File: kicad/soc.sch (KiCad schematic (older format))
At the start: 60 parts, among them J1 Line Out, J2 PS/2 Keyboard, J3 DB9, J4 Line In, J5 Headphone, P1 LED MATRIX, P2 ALTERA_DE1_GPIO, P3 IO, U1 SSM2603, U2 DS3234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

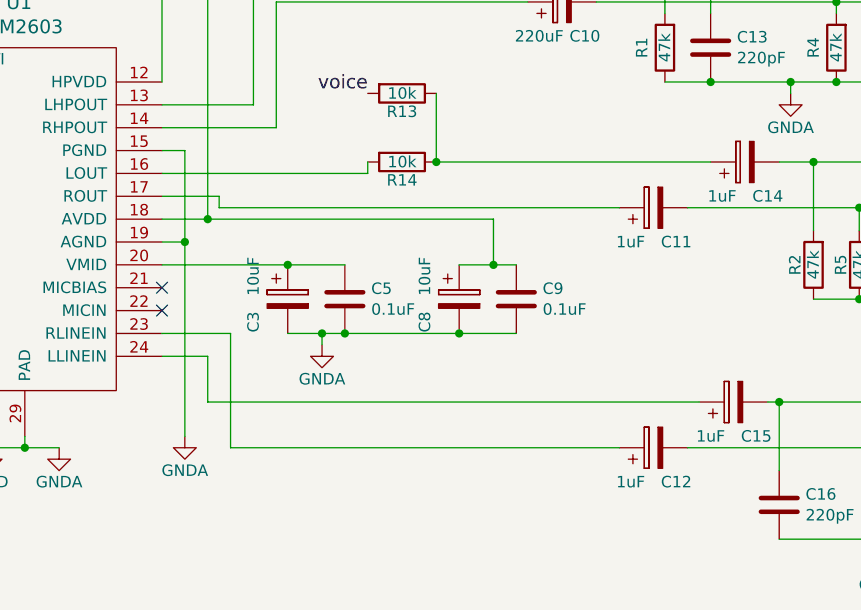
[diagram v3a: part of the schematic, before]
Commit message: additions to the support board
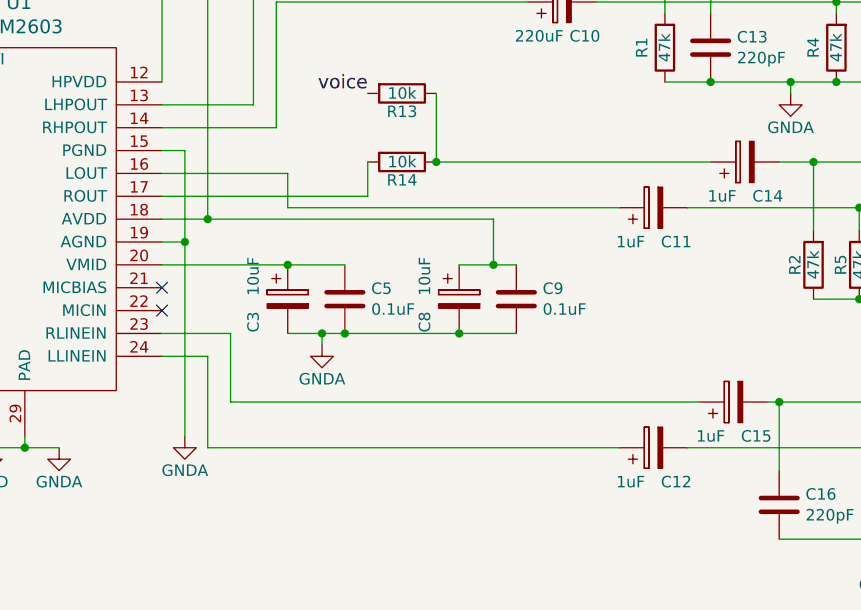
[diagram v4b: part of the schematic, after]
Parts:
- J3: footprint (none) -> mstock-pretty:DB9F
- J5: footprint (none) -> mstock-pretty:SJ-4351X-SMT
- U4: footprint (none) -> mstock-pretty:SOIC-16
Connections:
- net at U1.16 (LOUT): now also C11.1; no longer R14.2
- net at U1.17 (ROUT): now also R14.2; no longer C11.1
- net at U1.23 (RLINEIN): now also C15.1; no longer C12.1
- net at U1.24 (LLINEIN): now also C12.1; no longer C15.1
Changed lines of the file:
@@
 Connection ~ 8600 4300
 Wire Wire Line
-	5550 4150 6450 4150
-Wire Wire Line
-	5800 4300 7550 4300
-Wire Wire Line
-	5800 4300 5800 4250
-Wire Wire Line
-	5800 4250 5550 4250
+	6450 4250 5550 4250
 Wire Wire Line
 	7750 3750 9150 3750
@@
 Connection ~ 8700 5350
 Wire Wire Line
-	5750 5150 7900 5150
-Wire Wire Line
-	5850 5350 7550 5350
+	5750 5350 7550 5350
 Wire Wire Line
 	1750 2600 1250 2600
@@
 $EndComp
 Wire Wire Line
-	6450 4150 6450 4100
+	6450 4100 6450 4250
 Wire Wire Line
 	6750 3800 6750 4100
@@
 	5550 4850 5850 4850
 Wire Wire Line
-	5850 4850 5850 5350
-Wire Wire Line
 	5550 4950 5750 4950
 Wire Wire Line
-	5750 4950 5750 5150
+	5750 4950 5750 5350
 $Comp
 L MAX3232 U4
@@
 F 0 "U4" H 2000 7117 50  0000 C CNN
 F 1 "MAX3232" H 2000 7026 50  0000 C CNN
-F 2 "" H 2000 6150 50  0001 C CNN
+F 2 "mstock-pretty:SOIC-16" H 2000 6150 50  0001 C CNN
 F 3 "" H 2000 6150 50  0000 C CNN
 	1    2000 6150
@@
 F 0 "J3" H 3829 6796 50  0000 L CNN
 F 1 "DB9" H 3829 6705 50  0000 L CNN
-F 2 "" H 3650 6750 50  0001 C CNN
+F 2 "mstock-pretty:DB9F" H 3650 6750 50  0001 C CNN
 F 3 "" H 3650 6750 50  0000 C CNN
 	1    3650 6750
@@
 F 0 "J5" H 9650 3800 50  0000 R CNN
 F 1 "Headphone" H 9800 3100 50  0000 R CNN
-F 2 "" H 9750 3250 50  0001 C CNN
+F 2 "mstock-pretty:SJ-4351X-SMT" H 9750 3250 50  0001 C CNN
 F 3 "" H 9750 3250 50  0000 C CNN
 	1    9650 3400
@@
 Wire Wire Line
 	9150 3550 9150 3750
+Wire Wire Line
+	5850 4850 5850 5150
+Wire Wire Line
+	5850 5150 7900 5150
+Wire Wire Line
+	5550 4150 6100 4150
+Wire Wire Line
+	6100 4150 6100 4300
+Wire Wire Line
+	6100 4300 7550 4300
 $EndSCHEMATC

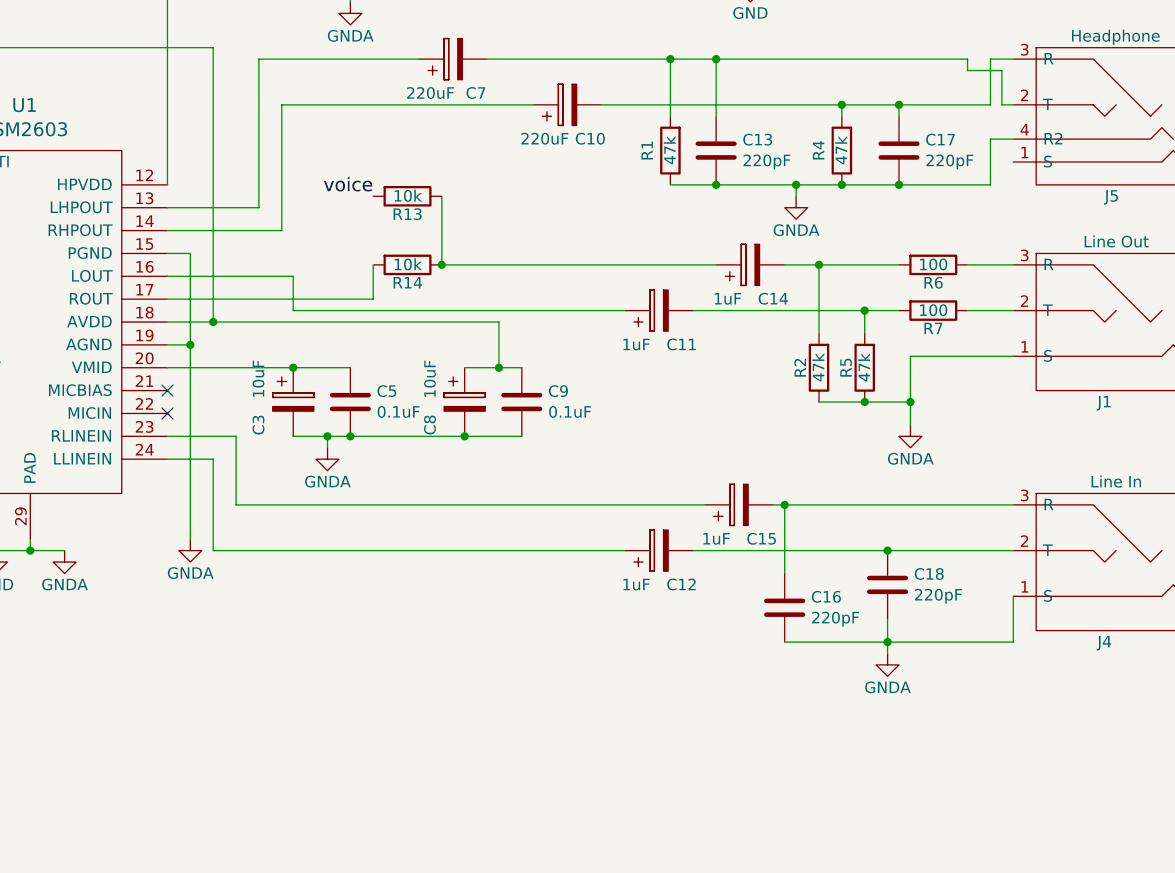
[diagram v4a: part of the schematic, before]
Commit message: adding mic input
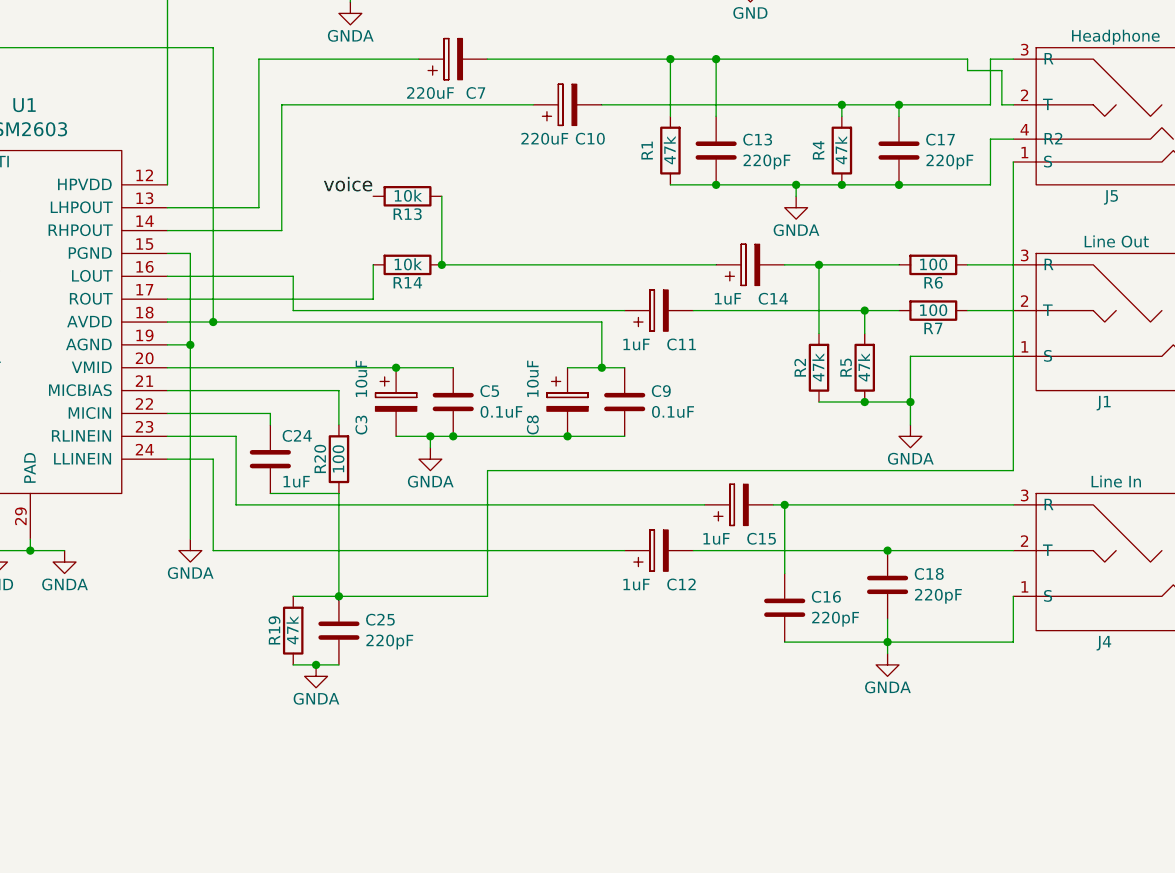
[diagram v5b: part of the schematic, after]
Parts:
- added C24: 1uF, Capacitors_SMD:C_0805_HandSoldering, symbol C
- added C25: 220pF, Capacitors_SMD:C_0805_HandSoldering, symbol C
- added R19: 47k, Resistors_SMD:R_0805_HandSoldering, symbol R
- added R20: 100, Resistors_SMD:R_0805_HandSoldering, symbol R
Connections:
- net GND: now also C25.1, R19.1
- net at U1.21 (MICBIAS): now also R20.2
- net at U1.22 (MICIN): now also C24.2
- net at J5.1 (S): now also C24.1, C25.2, R19.2, R20.1
- no-connect marks 19 -> 17
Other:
- moved on the sheet: C3, C5, C8, C9
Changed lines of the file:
@@
 L CP C3
 U 1 1 57F70C05
-P 6100 4700
-F 0 "C3" V 5950 4600 50  0000 C CNN
-F 1 "10uF" V 5950 4800 50  0000 C CNN
-F 2 "mstock:UWXCAP-3mm" H 6138 4550 50  0001 C CNN
-F 3 "" H 6100 4700 50  0000 C CNN
-	1    6100 4700
+P 6550 4700
+F 0 "C3" V 6400 4600 50  0000 C CNN
+F 1 "10uF" V 6400 4800 50  0000 C CNN
+F 2 "mstock:UWXCAP-3mm" H 6588 4550 50  0001 C CNN
+F 3 "" H 6550 4700 50  0000 C CNN
+	1    6550 4700
 	1    0    0    -1
 $EndComp
@@
 L C C5
 U 1 1 57F70CC1
-P 6350 4700
-F 0 "C5" H 6235 4654 50  0000 R CNN
-F 1 "0.1uF" H 6235 4745 50  0000 R CNN
-F 2 "Capacitors_SMD:C_0805_HandSoldering" H 6388 4550 50  0001 C CNN
-F 3 "" H 6350 4700 50  0000 C CNN
-	1    6350 4700
+P 6800 4700
+F 0 "C5" H 6685 4654 50  0000 R CNN
+F 1 "0.1uF" H 6685 4745 50  0000 R CNN
+F 2 "Capacitors_SMD:C_0805_HandSoldering" H 6838 4550 50  0001 C CNN
+F 3 "" H 6800 4700 50  0000 C CNN
+	1    6800 4700
 	-1   0    0    1
 $EndComp
@@
 L GNDA #PWR013
 U 1 1 57F70EBE
-P 6250 4900
-F 0 "#PWR013" H 6250 4650 50  0001 C CNN
-F 1 "GNDA" H 6250 4750 50  0000 C CNN
-F 2 "" H 6250 4900 50  0000 C CNN
-F 3 "" H 6250 4900 50  0000 C CNN
-	1    6250 4900
+P 6700 4900
+F 0 "#PWR013" H 6700 4650 50  0001 C CNN
+F 1 "GNDA" H 6700 4750 50  0000 C CNN
+F 2 "" H 6700 4900 50  0000 C CNN
+F 3 "" H 6700 4900 50  0000 C CNN
+	1    6700 4900
 	1    0    0    -1
 $EndComp
@@
 	1    0    0    -1
 $EndComp
-NoConn ~ 5550 4750
-NoConn ~ 5550 4650
 $Comp
 L GND #PWR016
@@
 L CP C8
 U 1 1 57F737E1
-P 6850 4700
-F 0 "C8" V 6700 4600 50  0000 C CNN
-F 1 "10uF" V 6700 4800 50  0000 C CNN
-F 2 "mstock:UWXCAP-3mm" H 6888 4550 50  0001 C CNN
-F 3 "" H 6850 4700 50  0000 C CNN
-	1    6850 4700
+P 7300 4700
+F 0 "C8" V 7150 4600 50  0000 C CNN
+F 1 "10uF" V 7150 4800 50  0000 C CNN
+F 2 "mstock:UWXCAP-3mm" H 7338 4550 50  0001 C CNN
+F 3 "" H 7300 4700 50  0000 C CNN
+	1    7300 4700
 	1    0    0    -1
 $EndComp
@@
 L C C9
 U 1 1 57F737E7
-P 7100 4700
-F 0 "C9" H 6985 4654 50  0000 R CNN
-F 1 "0.1uF" H 6985 4745 50  0000 R CNN
-F 2 "Capacitors_SMD:C_0805_HandSoldering" H 7138 4550 50  0001 C CNN
-F 3 "" H 7100 4700 50  0000 C CNN
-	1    7100 4700
+P 7550 4700
+F 0 "C9" H 7435 4654 50  0000 R CNN
+F 1 "0.1uF" H 7435 4745 50  0000 R CNN
+F 2 "Capacitors_SMD:C_0805_HandSoldering" H 7588 4550 50  0001 C CNN
+F 3 "" H 7550 4700 50  0000 C CNN
+	1    7550 4700
 	-1   0    0    1
 $EndComp
@@
 	6050 3950 5550 3950
 Wire Wire Line
-	5550 4550 6350 4550
-Connection ~ 6100 4550
-Wire Wire Line
-	6100 4850 7100 4850
-Wire Wire Line
-	6250 4850 6250 4900
-Connection ~ 6250 4850
+	5550 4550 6800 4550
+Connection ~ 6550 4550
+Wire Wire Line
+	6550 4850 7550 4850
+Wire Wire Line
+	6700 4850 6700 4900
+Connection ~ 6700 4850
 Wire Wire Line
 	3350 3950 4300 3950
@@
 	3750 3600 3750 3650
 Connection ~ 3750 3650
-Connection ~ 6350 4850
-Connection ~ 6850 4850
-Wire Wire Line
-	7100 4550 6850 4550
-Wire Wire Line
-	5550 4350 7000 4350
-Wire Wire Line
-	7000 4350 7000 4550
-Connection ~ 7000 4550
+Connection ~ 6800 4850
+Connection ~ 7300 4850
+Wire Wire Line
+	7550 4550 7300 4550
+Wire Wire Line
+	5550 4350 7450 4350
+Wire Wire Line
+	7450 4350 7450 4550
+Connection ~ 7450 4550
 Wire Wire Line
 	5750 4350 5750 3150
@@
 Wire Wire Line
 	6100 4300 7550 4300
+$Comp
+L R R19
+U 1 1 58574391
+P 6100 5700
+F 0 "R19" V 6180 5700 50  0000 C CNN
+F 1 "47k" V 6100 5700 50  0000 C CNN
+F 2 "Resistors_SMD:R_0805_HandSoldering" V 6030 5700 50  0001 C CNN
+F 3 "" H 6100 5700 50  0000 C CNN
+	1    6100 5700
+	-1   0    0    1
+$EndComp
+$Comp
+L GNDA #PWR032
+U 1 1 58574496
+P 6200 5850
+F 0 "#PWR032" H 6200 5600 50  0001 C CNN
+F 1 "GNDA" H 6200 5700 50  0000 C CNN
+F 2 "" H 6200 5850 50  0000 C CNN
+F 3 "" H 6200 5850 50  0000 C CNN
+	1    6200 5850
+	1    0    0    -1
+$EndComp
+$Comp
+L C C25
+U 1 1 58574558
+P 6300 5700
+F 0 "C25" H 6185 5654 50  0000 R CNN
+F 1 "220pF" H 6185 5745 50  0000 R CNN
+F 2 "Capacitors_SMD:C_0805_HandSoldering" H 6338 5550 50  0001 C CNN
+F 3 "" H 6300 5700 50  0000 C CNN
+	1    6300 5700
+	-1   0    0    1
+$EndComp
+Wire Wire Line
+	6100 5850 6300 5850
+Connection ~ 6200 5850
+Wire Wire Line
+	6100 5550 6950 5550
+Wire Wire Line
+	9250 3650 9250 5000
+Wire Wire Line
+	9250 5000 6950 5000
+Wire Wire Line
+	6950 5000 6950 5550
+Connection ~ 6300 5550
+$Comp
+L C C24
+U 1 1 58574C73
+P 6000 4950
+F 0 "C24" H 5950 4850 50  0000 R CNN
+F 1 "1uF" H 5950 5050 50  0000 R CNN
+F 2 "Capacitors_SMD:C_0805_HandSoldering" H 6038 4800 50  0001 C CNN
+F 3 "" H 6000 4950 50  0000 C CNN
+	1    6000 4950
+	-1   0    0    1
+$EndComp
+$Comp
+L R R20
+U 1 1 5857505E
+P 6300 4950
+F 0 "R20" V 6380 4950 50  0000 C CNN
+F 1 "100" V 6300 4950 50  0000 C CNN
+F 2 "Resistors_SMD:R_0805_HandSoldering" V 6230 4950 50  0001 C CNN
+F 3 "" H 6300 4950 50  0000 C CNN
+	1    6300 4950
+	-1   0    0    1
+$EndComp
+Wire Wire Line
+	5550 4650 6300 4650
+Wire Wire Line
+	6300 4650 6300 4800
+Wire Wire Line
+	5550 4750 6000 4750
+Wire Wire Line
+	6000 4750 6000 4800
+Wire Wire Line
+	6000 5100 6300 5100
+Wire Wire Line
+	6300 5100 6300 5550
 $EndSCHEMATC

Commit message: board layout progress, new SMT audio jacks
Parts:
- J1, J4: footprint mstock-pretty:SJI-3513N -> mstock-pretty:SJ-352X-SMT
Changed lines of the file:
@@
 F 0 "J1" H 9650 4700 50  0000 C CNN
 F 1 "Line Out" H 9600 4000 50  0000 C CNN
-F 2 "mstock-pretty:SJI-3513N" H 9750 4150 50  0001 C CNN
+F 2 "mstock-pretty:SJ-352X-SMT" H 9750 4150 50  0001 C CNN
 F 3 "" H 9750 4150 50  0000 C CNN
 	1    9650 4300
@@
 F 0 "J4" H 9650 5750 50  0000 C CNN
 F 1 "Line In" H 9600 5050 50  0000 C CNN
-F 2 "mstock-pretty:SJI-3513N" H 9750 5200 50  0001 C CNN
+F 2 "mstock-pretty:SJ-352X-SMT" H 9750 5200 50  0001 C CNN
 F 3 "" H 9750 5200 50  0000 C CNN
 	1    9650 5350
